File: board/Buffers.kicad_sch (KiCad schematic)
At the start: 17 parts, among them J26 Z Register, U20 74F541, U52 74F541, U53 74F245, U54 74F541, U55 74F541, U56 74F125, U62 74F541

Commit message: V2.0: wait states, GAL glue logic, serial clock and review fixes
Main board schematic:
- Replace the T4-T7 clock divider with RDY wait states. Fixed 7.16 MHz
  CPU clock; J36 selects 3.58 MHz for Rockwell parts. Waits are set per
  region through the write-only register at $FFF5 (reset = 3 waits).
- Move address decode, strobes, the wait-state generator, the IRQ
  encoder/latch/vector mux, ROM bank gating and DMA sync into seven GALs
  (U81-U86 ATF22V10C, U87 ATF16V8C), removing 29 ICs. CUPL sources,
  JEDECs and notes are in board/PLDs/V2.
- 1.8432 MHz serial clock, soft-power latch, -5V regulator, bulk caps,
  pull-ups, audio coupling/decoupling, GNDA tie, read-only Z register
  and other design-review fixes.
- New WaitStates and Support sheets; project symbol library
  hydra16.kicad_sym with sym-lib-table.

PCB updated from the schematic. Includes pending changes to the counter,
bus breakout and memory daughter card projects.

Firmware:
- Remove S_REGISTER; T/U/V/W now at $FFF0-$FFF3 to match the hardware.
- Add math.s and sound.s (included by os_main.s).
- Rebuild the 65C02 ROM image.

Co-Authored-By: Claude Opus 5.5 <noreply@anthropic.com>
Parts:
- removed RN5: 103, Resistor_THT:R_Array_SIP9, symbol Device:R_Network08_US
- removed U20: 74F541, Package_DIP:DIP-20_W7.62mm_Socket_LongPads, symbol 74xx:74LS541
- U55: value 74F541 -> 74HCT541
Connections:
- net DDIR_S is gone; now on net !RWB: U53.1 (A->B)
- net +5V: no longer U56.13
- net GND: now also U56.13
- net RWB: no longer U56.5
- net nFFF4_S renamed nZREG_RD
- new net nWR_Q: U56.5

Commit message: V2.0 rev 2.0D: clock stretching, OS ROM paging and review fixes
Bus timing:
- New GAL C (U88) generates PHI2/PHI1 and the 3.58 MHz sound clock from
  the 14.318 MHz master, replacing the U35 74F191 divider. J36 now selects
  7.16 or 3.58 MHz.
- Banked RAM, banked ROM and slot I/O ($FF20-$FFEF) get one extra PHI2-low
  period plus 0-3 extra PHI2-high periods set in $FFF5 (GAL D). This
  replaces the on-board RDY wait generator; cards can still pull RDY.
- Write strobes are now hold-time safe: PHI1 comes straight from GAL C
  and RWB_M straight from GAL B2.

Review fixes:
- OS ROM chip enable from a single-level decode, output enable from
  GAL B1; -55 part specified. Full 4K OS ROM paging via GAL G.
- Vector RAM writes only during PHI2; $FFF0-$FFFF no longer slowed.
- YM2151 /WR on RWB_M. U62 removed. RB0-RB7 pull-ups (RN5).
- Slot clocks driven through U56 and U34 with 33R series resistors.
- J38 enables in-system flashing of the banked ROMs.
- W65C22S/W65C51N, AS6C4008, DS1813-5 and CY7C192-25 values; R4 1k.
- J7 pin 8 no longer +5V; +5VA renamed +5VSB; serial handshake loop.
- Sheet titles and revisions, slot symbol pin fixes, and project symbol
  and footprint libraries so the project opens on another machine.

Co-Authored-By: Claude Opus 5.5 <noreply@anthropic.com>
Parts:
- removed U62: 74F541, Package_DIP:DIP-20_W7.62mm_Socket_LongPads, symbol 74xx:74LS541
- added R21, R22, R23: 33, Resistor_THT:R_Axial_DIN0204_L3.6mm_D1.6mm_P5.08mm_Horizontal, symbol Device:R
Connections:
- net nWR_Q is gone; now on net PHI2: U56.5
- net !RWB: no longer U56.9
- net PHI2: no longer U56.11
- net !RWB_M renamed PHI1_DRV
- net PHI1_DRV: now also R22.1
- net RWB_M renamed PHI2_DRV
- net PHI2_DRV: now also R21.1
- net X_PHI2 renamed SND_CLK
- new net PHI1: U56.9
- new net PHI1_BUS: R22.2
- new net PHI2_BUS: R21.2
- new net SND_CLK_BUS: R23.2
- new net SND_DRV: R23.1, U56.11
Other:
- title: ZeroPage $00/$01 Mirror Memory and RAM/ROM Bank Logic -> CPU Bus Buffers and Slot Clock Drivers

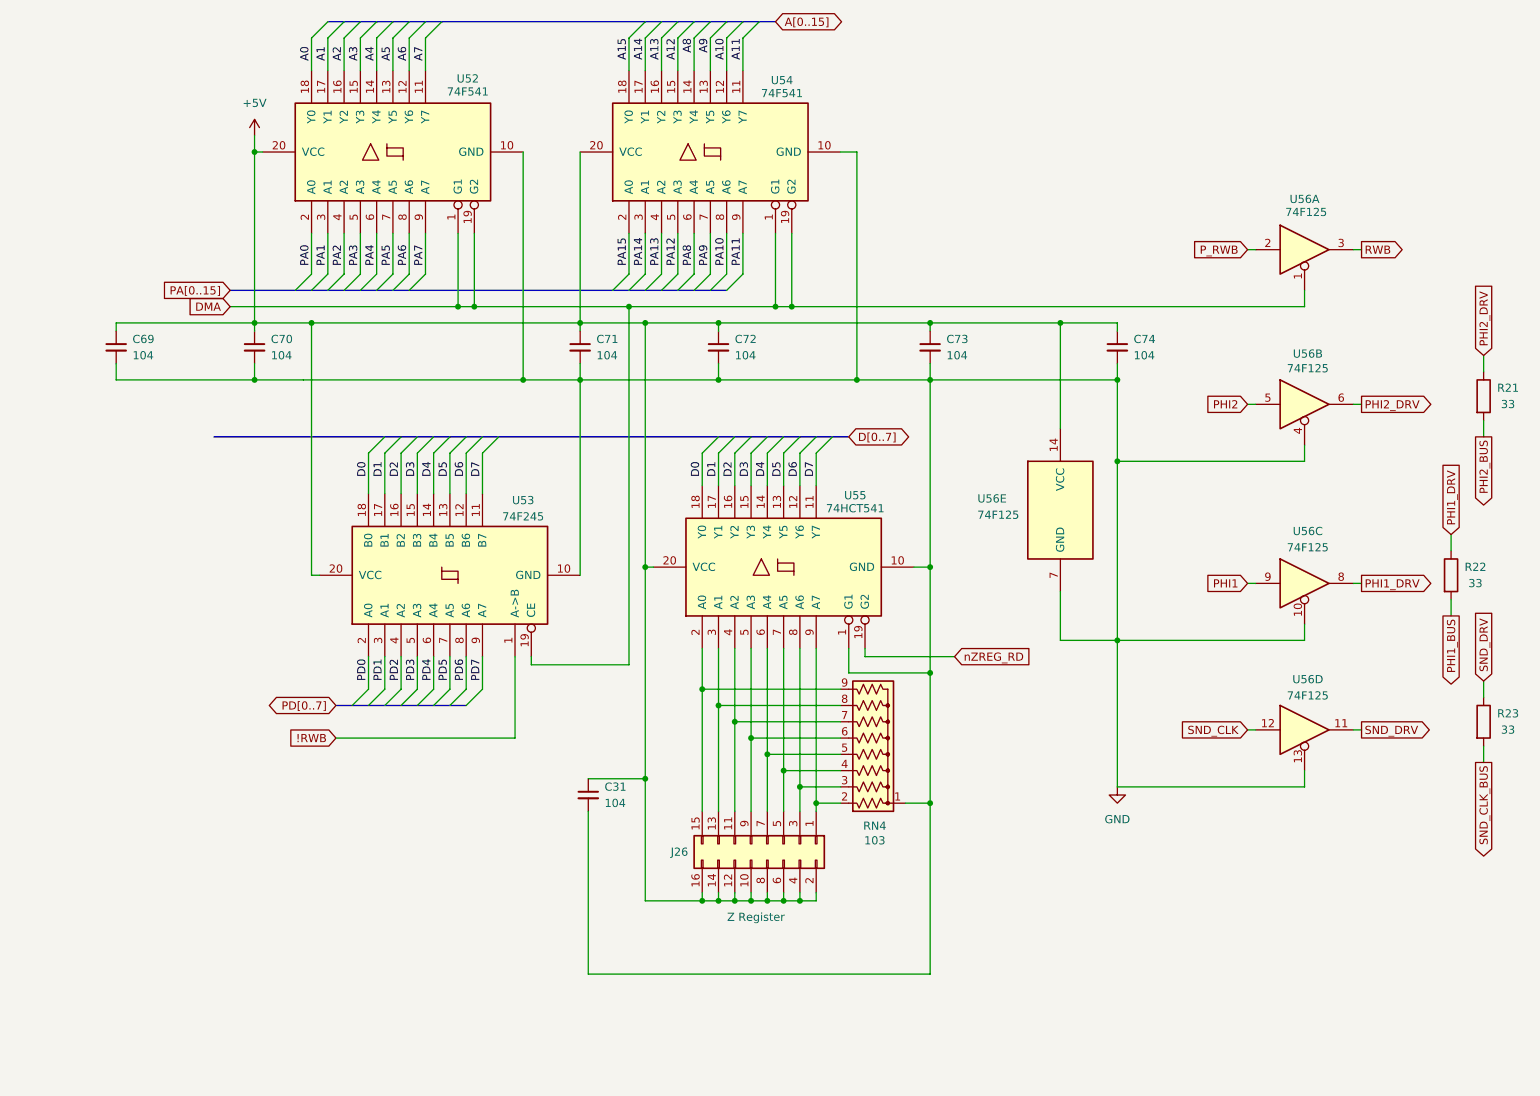
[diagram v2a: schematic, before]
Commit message: V2.0: split Support sheet, add stereo amplifier and on-board speakers
Support sheet reorganized (connectivity unchanged):
- Support.kicad_sch renamed to Power: ATX, front panel, reset, soft power, -5V
- Oscillators and their parts moved to Clocks (now US Ledger)
- Sound-chip decoupling and line-out parts moved to Sound
- VIA CB1/CB2/SPI pull-ups moved to Connectors
- Also includes minor schematic edits made before the reorganization

Audio output rework (Sound, now A3):
- U89 TDA2822M stereo amplifier on 9 V from U90 L7809 (fed by +12V)
- RV1 dual 10k log volume pot behind R26/R27 220k attenuators
- J18 moved from Connectors and now uses the switched TRS symbol:
  a plug lifts T/R off TN/RN and mutes the on-board speakers
- LS1/LS2 8 ohm mini speakers through R30/R31 (15R 0.5 W)
- New footprint Speaker_D32mm_P15.24mm_P17.50mm (two pad pairs, fits
  Adafruit 1898 or Kitronik 3316)
- J39 line-out header (LINE_L, LINE_R, GNDA)
- R18 stays the single GNDA-GND tie, to sit at U89 pin 4
- TDA2822M symbol added to hydra16.kicad_sym

Co-Authored-By: Claude Opus 5.5 <noreply@anthropic.com>
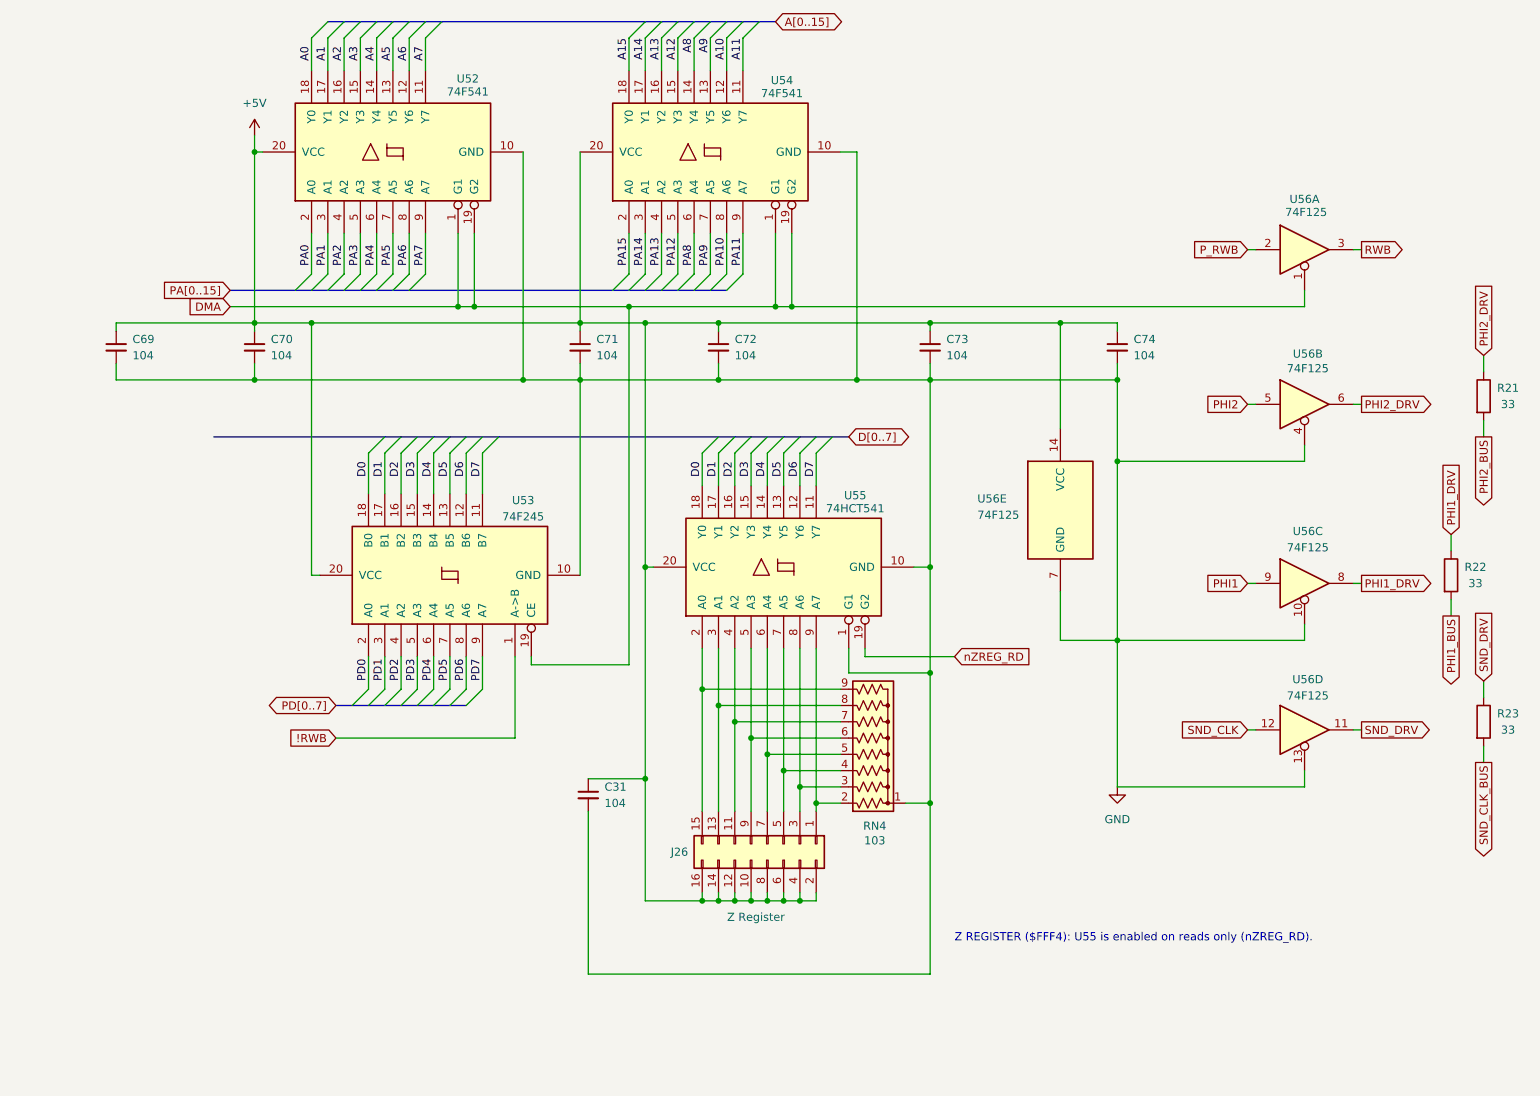
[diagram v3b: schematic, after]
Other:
- note added: "Z REGISTER ($FFF4): U55 is enabled on reads only (nZREG_RD)."

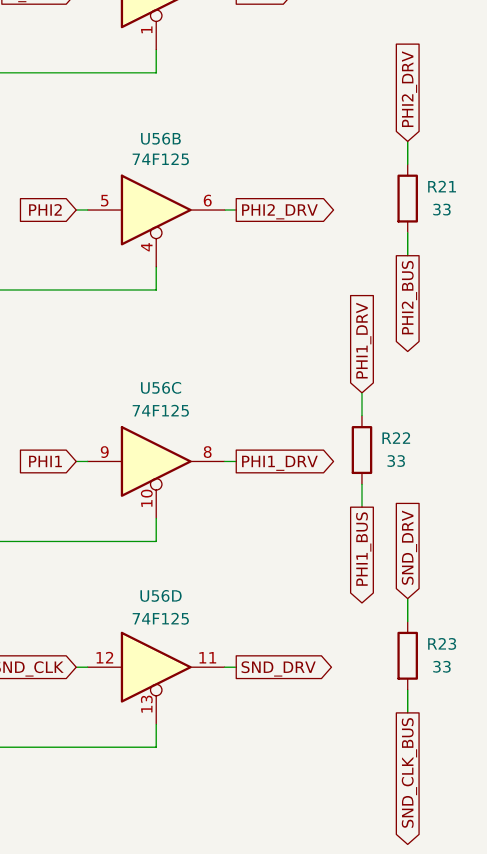
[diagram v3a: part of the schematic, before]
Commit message: V2.0: consolidate parts (239 -> 216), GAL C rev 02
No change in function:
- U9 74F08 removed: GAL C (U88) rev 02 makes the CPU phi0 (P_PHI0 = PHI2
  held low while DMAB_S is low); its decoupling cap C14 removed
- U34 74ACT14 removed: the two clock buffers use spare U19 74F240 gates
- U60 + U61 (2 x CY7C192 vector RAM) replaced by one AS7C256B-15
  (32K x 8, 15 ns); the IRQ sheet's D[0..7] bus is gone
- Crystal oscillators (U75 74HCU04, Y1, Y2, R1, R6-R8, C43, C44, C96,
  C97) replaced by canned oscillators X1 (14.31818 MHz), X2 (1.8432 MHz)
- Soft power: CD40106 -> 74HC14, CD4013 -> 74HC74 (active-low set/reset,
  power-on reset network inverted); a spare 74HC14 gate drives PS_ON#,
  so Q1 is removed
- R10-R13 -> RN6 (4 x 10k, SIP-5); R9, R21-R24 -> RN7 (5 x 33R isolated,
  SIP-10)
- C100-C102 (3 x 220u) -> C100 680u
- Clocks and Power sheet notes updated; PLD README updated

GAL C rev 02 verified against rev 01 over 200,000 clock edges.
PCB updated from the schematic (adds RN6, RN7, X1, X2 and the speakers
LS1/LS2). Also includes KiCad's re-save of the schematic sheets.

Co-Authored-By: Claude Opus 5.5 <noreply@anthropic.com>
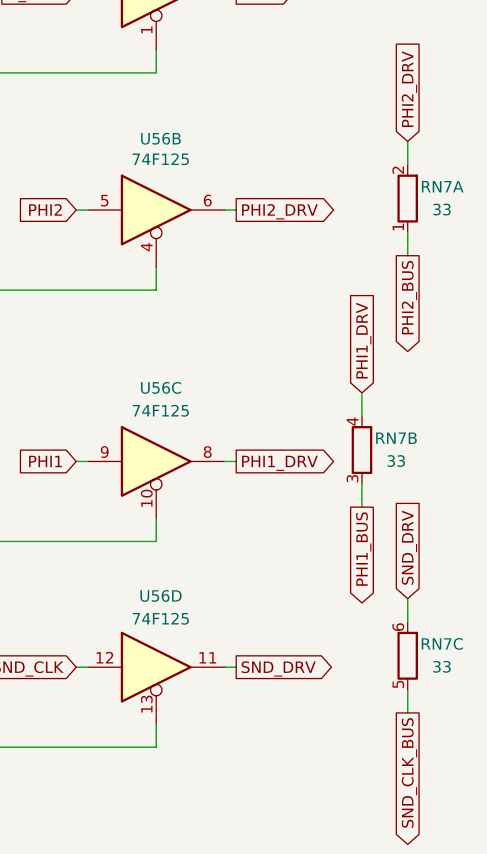
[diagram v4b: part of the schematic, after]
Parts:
- removed R22, R23: 33, Resistor_THT:R_Axial_DIN0204_L3.6mm_D1.6mm_P5.08mm_Horizontal, symbol Device:R
- added unit 2 of RN7
- added unit 3 of RN7
- RN7: renamed from R21; footprint Resistor_THT:R_Axial_DIN0204_L3.6mm_D1.6mm_P5.08mm_Horizontal -> Resistor_THT:R_Array_SIP10; symbol Device:R -> Device:R_Pack05_SIP_Split
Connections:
- net PHI1_BUS: now also RN7.3 (R2.1)
- net PHI1_DRV: now also RN7.4 (R2.2)
- net PHI2_BUS: now also RN7.1 (R1.1); no longer RN7.2
- net PHI2_DRV: now also RN7.2 (R1.2); no longer RN7.1
- net SND_CLK_BUS: now also RN7.5 (R3.1)
- net SND_DRV: now also RN7.6 (R3.2)
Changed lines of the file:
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@@
 		(comment 1 "Hydra 16")
 	)
+	(text "Z REGISTER ($FFF4): U55 is enabled on reads only (nZREG_RD)."
+		(exclude_from_sim no)
+		(at 162.56 163.83 0)
+		(effects
+			(font
+				(size 1.27 1.27)
+			)
+			(justify left top)
+		)
+	)
 	(junction
 		(at 87.63 66.04)
@@
 	)
 	(symbol
-		(lib_id "Device:R")
+		(lib_id "Device:R_Pack05_SIP_Split")
 		(at 245.11 80.01 0)
 		(unit 1)
@@
 		(on_board yes)
 		(dnp no)
-		(property "Reference" "R21"
+		(property "Reference" "RN7"
 			(at 248.92 78.74 0)
 			(effects
@@
 			)
 		)
-		(property "Footprint" "Resistor_THT:R_Axial_DIN0204_L3.6mm_D1.6mm_P5.08mm_Horizontal"
+		(property "Footprint" "Resistor_THT:R_Array_SIP10"
 			(at 245.11 80.01 0)
 			(effects
@@
 			)
 		)
-		(property "Datasheet" ""
+		(property "Datasheet" "~"
 			(at 245.11 80.01 0)
 			(effects
@@
 			)
 		)
-		(property "Description" ""
+		(property "Description" "5 isolated resistors, SIP-10: 33R series terminations for the slot clocks"
 			(at 245.11 80.01 0)
 			(effects
@@
 			)
 		)
-		(pin "1"
-		)
 		(pin "2"
 		)
+		(pin "1"
+		)
 		(instances
 			(project "hydra-16"
 				(path "/ef29fc71-3fec-48b5-8a1a-46bee537a98c/be1fd2da-2765-4044-ae46-297533c36c50"
-					(reference "R21")
+					(reference "RN7")
 					(unit 1)
 				)
@@
 	)
 	(symbol
-		(lib_id "Device:R")
+		(lib_id "Device:R_Pack05_SIP_Split")
 		(at 245.11 130.81 0)
-		(unit 1)
+		(unit 3)
 		(exclude_from_sim no)
 		(in_bom yes)
 		(on_board yes)
 		(dnp no)
-		(property "Reference" "R23"
+		(property "Reference" "RN7"
 			(at 248.92 129.54 0)
 			(effects
@@
 			)
 		)
-		(property "Footprint" "Resistor_THT:R_Axial_DIN0204_L3.6mm_D1.6mm_P5.08mm_Horizontal"
+		(property "Footprint" "Resistor_THT:R_Array_SIP10"
 			(at 245.11 130.81 0)
 			(effects
@@
 			)
 		)
-		(property "Datasheet" ""
+		(property "Datasheet" "~"
 			(at 245.11 130.81 0)
 			(effects
@@
 			)
 		)
-		(property "Description" ""
+		(property "Description" "5 isolated resistors, SIP-10: 33R series terminations for the slot clocks"
 			(at 245.11 130.81 0)
 			(effects
@@
 			)
 		)
-		(pin "1"
+		(pin "6"
 		)
-		(pin "2"
+		(pin "5"
 		)
 		(instances
 			(project "hydra-16"
 				(path "/ef29fc71-3fec-48b5-8a1a-46bee537a98c/be1fd2da-2765-4044-ae46-297533c36c50"
-					(reference "R23")
-					(unit 1)
+					(reference "RN7")
+					(unit 3)
 				)
 			)
@@
 	)
 	(symbol
-		(lib_id "Device:R")
+		(lib_id "Device:R_Pack05_SIP_Split")
 		(at 240.03 107.95 0)
-		(unit 1)
+		(unit 2)
 		(exclude_from_sim no)
 		(in_bom yes)
 		(on_board yes)
 		(dnp no)
-		(property "Reference" "R22"
+		(property "Reference" "RN7"
 			(at 243.84 106.68 0)
 			(effects
@@
 			)
 		)
-		(property "Footprint" "Resistor_THT:R_Axial_DIN0204_L3.6mm_D1.6mm_P5.08mm_Horizontal"
+		(property "Footprint" "Resistor_THT:R_Array_SIP10"
 			(at 240.03 107.95 0)
 			(effects
@@
 			)
 		)
-		(property "Datasheet" ""
+		(property "Datasheet" "~"
 			(at 240.03 107.95 0)
 			(effects
@@
 			)
 		)
-		(property "Description" ""
+		(property "Description" "5 isolated resistors, SIP-10: 33R series terminations for the slot clocks"
 			(at 240.03 107.95 0)
 			(effects
@@
 			)
 		)
-		(pin "1"
+		(pin "4"
 		)
-		(pin "2"
+		(pin "3"
 		)
 		(instances
 			(project "hydra-16"
 				(path "/ef29fc71-3fec-48b5-8a1a-46bee537a98c/be1fd2da-2765-4044-ae46-297533c36c50"
-					(reference "R22")
-					(unit 1)
+					(reference "RN7")
+					(unit 2)
 				)
 			)
 		)
 	)
-	(text "Z REGISTER ($FFF4): U55 is enabled on reads only (nZREG_RD)."
-		(exclude_from_sim no)
-		(at 162.56 163.83 0)
-		(effects
-			(font
-				(size 1.27 1.27)
-			)
-			(justify left top)
-		)
-	)
